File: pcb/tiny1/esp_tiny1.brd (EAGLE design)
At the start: 45 x 95 mm, 35 parts, among them IC1 4000D, Q1 BUZ11BH

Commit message: added tiny board
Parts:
- removed D3: ES2D, diode:SMB
- removed DHT22: TEMP-HUM-SENSOR-DHT22, diy-modules:TEMP-HUM-SENSOR-DHT22
- removed ESP: ESP12E_DEVKIT, ESP12E_DEVKIT:ESP12E_DEVKIT
- removed IC1: 4000D, 40xx:SO14
- removed LDO: REG1117, burr-brown:SOT223
- removed PIR: MOTION-PIR-DYP-ME003, diy-modules:MOTION-PIR-DYP-ME003
- removed Q1: BUZ11BH, transistor-power:TO220BH
- removed SV2, SV3: (no value), con-lstb:MA03-1
- removed TP1: TPTP20SQ, testpad:TP20SQ
- removed U$5, U$6: SMD_SJ_3WAY_CLOSED, JKW_CHIP:SMD_SJ_3WAY_CLOSED
- added D1: (no value), SparkFun-LED:WS2812B
- added DS_GND, DS_SIG, DS_VCC: (no value), wirepad:SMD1,27-2,54
- added PIR1: MOTION-PIR-DYP-ME003, diy-modules:MOTION-PIR-DYP-ME003_FRAMELESS
- added R4, R5, R6: 10k, rcl:M0805
- added S1: TAC_SWITCHSMD, SparkFun-Retired:TACTILE-SWITCH-SMD
- added U1: (no value), esp8266modules:ESP12-SMD
- U$12: value MP1584EN_FRAMELESS -> MP1584EN; device JKW_CHIP:MP1584EN_FRAMELESS -> JKW_CHIP:MP1584EN
- moved U$4 104.6 mm to (96.2, 22.7)
- moved SV4 98.5 mm to (87.2, 37.2), turned to 270 degrees
- moved R1 97.9 mm to (94.8, 37.5)
- moved T_DIM1 94.0 mm to (100.0, 12.5), turned to 0 degrees
- moved U$11 88.6 mm to (62.8, 13.6)
- moved U$9 85.8 mm to (79.6, 23.7), flipped to the top
- moved DP2 80.5 mm to (93.5, 13.5), turned to 180 degrees
- moved SV1 76.6 mm to (67.5, 41.8), flipped to the bottom, turned to 0 degrees
- moved RELAY1 76.6 mm to (68.0, 18.9), turned to 270 degrees
- moved T_DIM2 74.7 mm to (92.5, 12.5), turned to 0 degrees
- moved D8 70.8 mm to (77.6, 20.1)
- moved U$3 70.0 mm to (100.0, 4.50), turned to 0 degrees
- moved U$1 61.5 mm to (80.7, 28.9)
- moved U$8 59.5 mm to (60.0, 4.50), turned to 0 degrees
- moved DP3 59.0 mm to (85.1, 13.5), turned to 180 degrees
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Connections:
- removed net DIMM2: DP2.1, ESP.D1, ESP.D11
- removed net N$12: ESP.EN, ESP.EN1
- removed net N$13: ESP.RST, ESP.RST1
- removed net N$14: D3.A, ESP.RSV@1, ESP.RSV@11
- removed net N$24: PIR.4, U$5.1
- removed net N$31: PIR.1, U$6.3
- removed net PIR: ESP.D3, ESP.D31, PIR.2
- removed net RERLAY: ESP.D6, ESP.D61, RELAY.1
- new net A_IN: U$3.P$2, U1.ADC
- new net N$5: PIR1.2, U1.GPIO14
- new net N$6: SV1.2, U1.RXD0
- new net N$7: S1.1, U1.GPIO0
- new net RELAY: RELAY.1, U1.GPIO12
- net DHT_SIG/SDA: now also U1.GPIO2; no longer DHT22.2, ESP.D4, ESP.D41
- net DIMM1: now also U1.GPIO4; no longer ESP.D2, ESP.D21, IC1.5, Q1.G
- net DIMM3: now also D1.4, U1.GPIO16; no longer ESP.D0, ESP.D01, IC1.3
- net DIMMING1: no longer Q1.D
- net EARTH_HUM_POW: now also R5.1, U1.GPIO15; no longer ESP.D8, ESP.D81
- net GND: now also D1.3, DS_GND.1, PIR1.3, R5.2, S1.3, SV1.1, U1.GND; no longer DHT22.4, ESP.GND@0, ESP.GND@1, ESP.GND@2, ESP.GND@3, ESP.GND@4, ESP.GND@5, ESP.GND@6, ESP.GND@7, IC1.7, LDO.1, PIR.3, Q1.S, SV1.3, SV2.3, SV3.3
- net N$1: now also R6.1, U1.CH_PD; no longer ESP.AD0, ESP.AD1, U$3.P$2
- net N$17: no longer LDO.3
- net N$2: now also R4.1, U1.RESET; no longer ESP.RSV@0, ESP.RSV@01
- net N$4: now also SV1.3, U1.TXD0; no longer IC1.6, TP1.TP
- net ONEWIRE_DS12B20: now also DS_SIG.1, U1.GPIO13; no longer ESP.D7, ESP.D71, SV1.2, SV2.2, SV3.2
- net SCL: now also DP2.1, U1.GPIO5; no longer ESP.D5, ESP.D51
- net VCC: now also PIR1.1; no longer D3.C, D8.C, ESP.VIN, ESP.VIN1, LDO.2, RELAY1.COIL0, U$12.VOUT, U$6.2
- net VDD: now also D1.1, D8.C, DS_VCC.1, PIR1.4, R4.2, R6.2, RELAY1.COIL0, U$12.VOUT, U1.VCC; no longer DHT22.1, ESP.3V3@0, ESP.3V3@1, ESP.3V3@2, ESP.3V3@3, ESP.3V3@4, ESP.3V3@5, IC1.14, SV1.1, SV2.1, SV3.1, U$5.2
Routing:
- net VCC: track 123.5 -> 0.00 mm, vias 4 -> 0
- net DHT_SIG/SDA: track 138.4 -> 20.4 mm, vias 2 -> 1
- net VDD: track 194.7 -> 94.9 mm, vias 3 -> 1
- net A_IN: track 0.00 -> 81.1 mm
- net ONEWIRE_DS12B20: track 94.0 -> 28.7 mm, vias 5 -> 0
- net GND: track 64.1 -> 5.33 mm, vias 15 -> 3
- net PIR: track 58.3 -> 0.00 mm, vias 3 -> 0
- net DIMM2: track 58.3 -> 0.00 mm, vias 2 -> 0
- net DIMMING1: track 69.3 -> 11.6 mm
- net N$1: track 42.2 -> 4.45 mm
- net EARTH_HUM_POW: track 12.2 -> 47.8 mm, vias 0 -> 1
- net NORMALLY_OPEN: track 40.1 -> 7.55 mm
- net RERLAY: track 31.4 -> 0.00 mm, vias 1 -> 0
- net DIMMING2: track 40.4 -> 10.6 mm
- net SCL: track 82.5 -> 57.9 mm
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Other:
- board size 45 x 95 mm -> 50 x 50 mm
- board text added: "SMARTHOME ESPtiny v01 | 2017"
- board text removed: "DIM1"
- board text removed: "DIM2"
- board text removed: "DIM3"
- board text removed: "POWER VIA 3V"
- board text removed: "POWER VIA VIN"
- board text removed: "SIG"
- board text removed: "SMARTHOME ESP MQTT v03 | 2017"

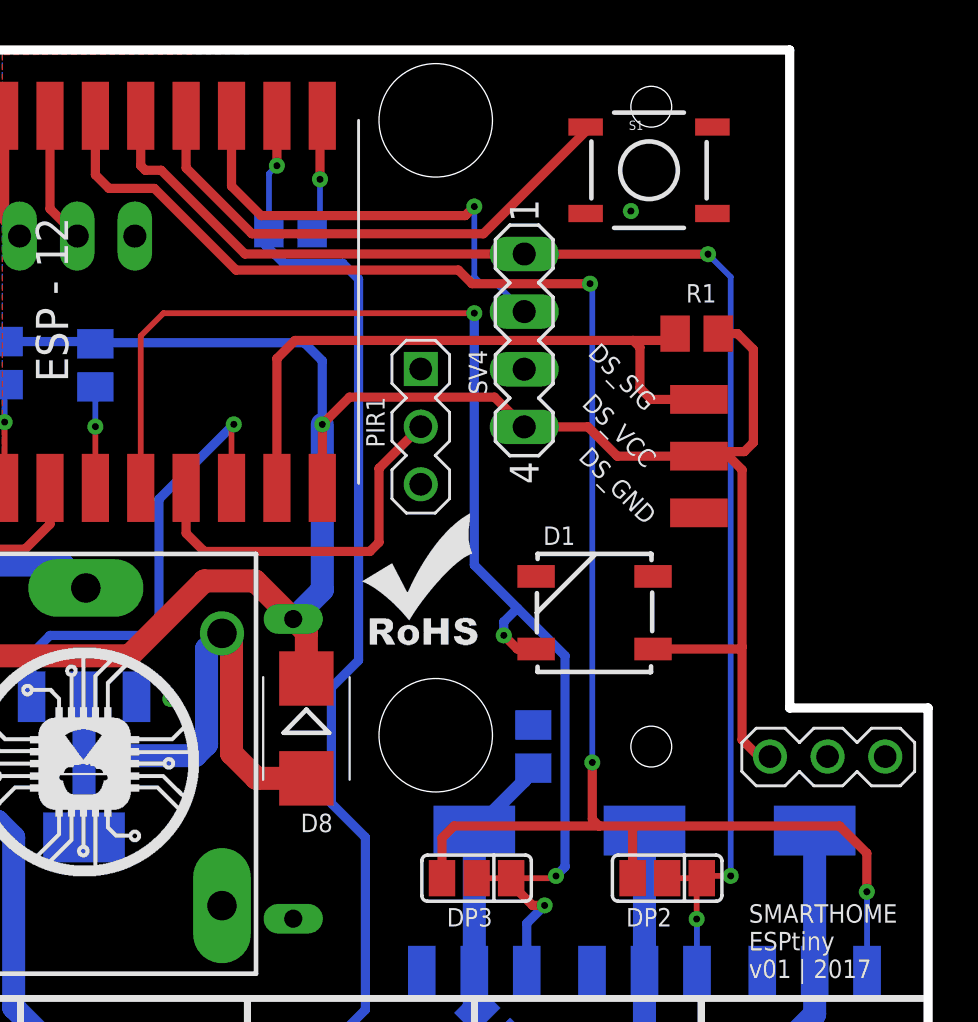
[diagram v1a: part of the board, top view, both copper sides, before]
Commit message: fixed i2c error, thanks to michell
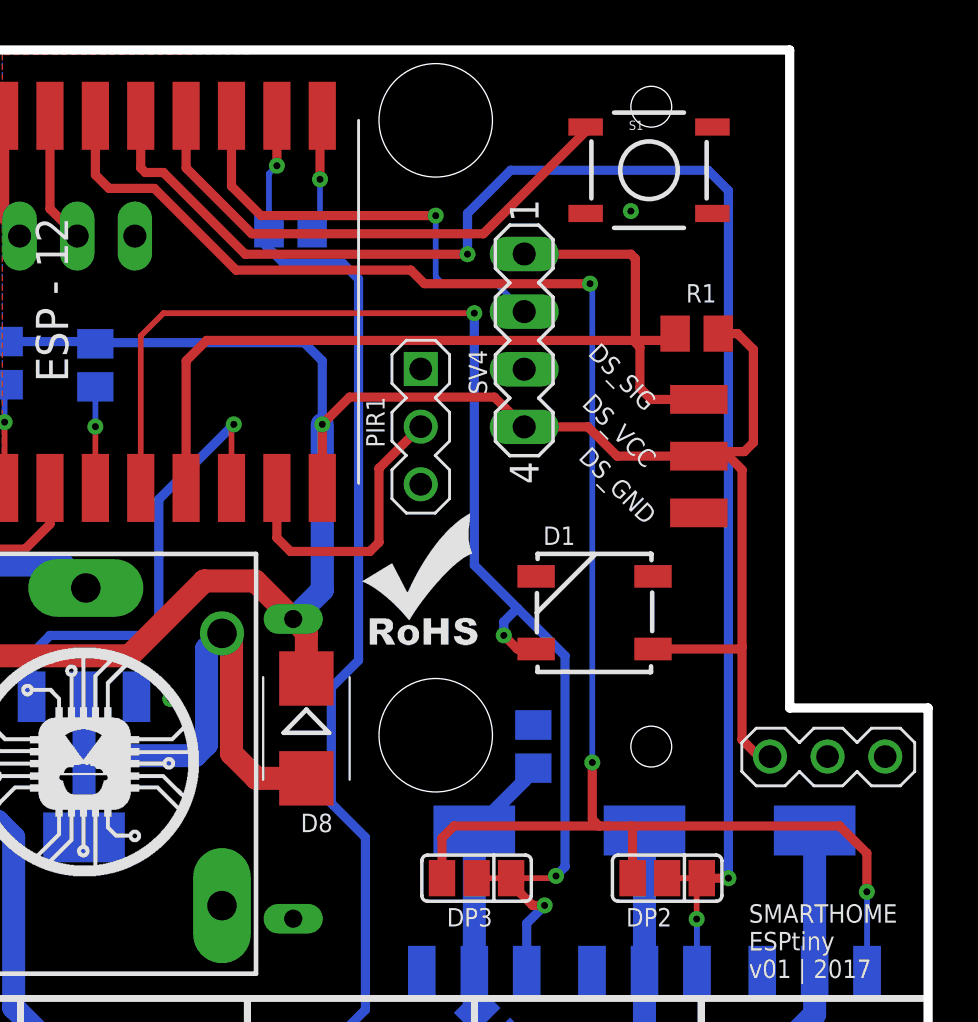
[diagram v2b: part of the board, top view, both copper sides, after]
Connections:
- removed net N$5: PIR1.2, U1.GPIO14
- removed net ONEWIRE_DS12B20: DS_SIG.1, R1.1, U1.GPIO13
- new net N$8: DP2.1, U1.GPIO5
- new net PIR: PIR1.2, U1.GPIO13
- net SCL: now also DS_SIG.1, R1.1, U1.GPIO14; no longer DP2.1, U1.GPIO5
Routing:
- net N$8: track 0.00 -> 64.2 mm, vias 0 -> 2
- net ONEWIRE_DS12B20: track 28.7 -> 0.00 mm
- net N$5: track 16.9 -> 0.00 mm
- net SCL: track 57.9 -> 41.3 mm, vias 2 -> 0
- net PIR: track 0.00 -> 13.0 mm
- net DHT_SIG/SDA: track 20.4 -> 19.9 mm
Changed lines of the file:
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@@
 <contactref element="SV4" pad="2"/>
 <contactref element="U1" pad="GPIO2"/>
-<via x="85" y="43.1" extent="1-16" drill="0.3048"/>
-<wire x1="85" y1="43.1" x2="85" y2="40" width="0.254" layer="16"/>
-<wire x1="85" y1="40" x2="85.3" y2="39.7" width="0.254" layer="16"/>
-<wire x1="85.3" y1="39.7" x2="85.97" y2="39.7" width="0.254" layer="16"/>
+<via x="83.3" y="42.7" extent="1-16" drill="0.3048"/>
 <wire x1="85.97" y1="39.7" x2="87.2" y2="38.47" width="0.254" layer="16"/>
 <wire x1="74.3" y1="47.1" x2="74.3" y2="44" width="0.4064" layer="1"/>
 <wire x1="74.3" y1="44" x2="75.6" y2="42.7" width="0.4064" layer="1"/>
-<wire x1="75.6" y1="42.7" x2="84.6" y2="42.7" width="0.4064" layer="1"/>
-<wire x1="84.6" y1="42.7" x2="85" y2="43.1" width="0.4064" layer="1"/>
+<wire x1="75.6" y1="42.7" x2="83.3" y2="42.7" width="0.4064" layer="1"/>
+<wire x1="85.97" y1="39.7" x2="83.6" y2="39.7" width="0.254" layer="16"/>
+<wire x1="83.6" y1="39.7" x2="83.3" y2="40" width="0.254" layer="16"/>
+<wire x1="83.3" y1="40" x2="83.3" y2="42.7" width="0.254" layer="16"/>
 </signal>
 <signal name="DIMM1">
@@
 <wire x1="83.576" y1="15.276" x2="84.1" y2="15.8" width="0.4064" layer="1"/>
 <wire x1="84.1" y1="15.8" x2="90.5" y2="15.8" width="0.4064" layer="1"/>
-<wire x1="90.5" y1="15.8" x2="101.1" y2="15.8" width="0.4064" layer="1"/>
+<wire x1="90.5" y1="15.8" x2="90.9" y2="15.8" width="0.4064" layer="1"/>
+<wire x1="91.9" y1="15.8" x2="101.1" y2="15.8" width="0.4064" layer="1"/>
 <wire x1="101.1" y1="15.8" x2="102.3" y2="14.6" width="0.4064" layer="1"/>
 <wire x1="90.2" y1="18.6" x2="90.2" y2="16.1" width="0.4064" layer="1"/>
@@
 <wire x1="68.9" y1="43.9" x2="70.9" y2="43.9" width="0.4064" layer="1"/>
 <wire x1="70.9" y1="43.9" x2="74.5" y2="40.3" width="0.4064" layer="1"/>
-<wire x1="74.5" y1="40.3" x2="84.3" y2="40.3" width="0.4064" layer="1"/>
-<wire x1="84.3" y1="40.3" x2="84.9" y2="39.7" width="0.4064" layer="1"/>
-<wire x1="84.9" y1="39.7" x2="90.1" y2="39.7" width="0.4064" layer="1"/>
-<wire x1="90.5" y1="15.8" x2="91.9" y2="15.8" width="0" layer="19" extent="1-1"/>
+<wire x1="74.5" y1="40.3" x2="82.2" y2="40.3" width="0.4064" layer="1"/>
+<wire x1="82.2" y1="40.3" x2="82.8" y2="39.7" width="0.4064" layer="1"/>
+<wire x1="82.8" y1="39.7" x2="90.1" y2="39.7" width="0.4064" layer="1"/>
+<wire x1="91.9" y1="15.8" x2="90.9" y2="15.8" width="0.4064" layer="1"/>
 </signal>
 <signal name="DIMM3">
@@
 <wire x1="97.5" y1="5" x2="100" y2="7.5" width="1.016" layer="16"/>
 <wire x1="100" y1="7.5" x2="100" y2="9.401" width="1.016" layer="16"/>
-</signal>
-<signal name="ONEWIRE_DS12B20">
-<contactref element="R1" pad="1"/>
-<contactref element="U1" pad="GPIO13"/>
-<contactref element="DS_SIG" pad="1"/>
-<wire x1="76.3" y1="30.7" x2="76.3" y2="36.4" width="0.4064" layer="1"/>
-<wire x1="76.3" y1="36.4" x2="77.1" y2="37.2" width="0.4064" layer="1"/>
-<wire x1="77.1" y1="37.2" x2="92" y2="37.2" width="0.4064" layer="1"/>
-<wire x1="92" y1="37.2" x2="93.55" y2="37.2" width="0.4064" layer="1"/>
-<wire x1="93.55" y1="37.2" x2="93.85" y2="37.5" width="0.4064" layer="1"/>
-<wire x1="94.9" y1="34.6" x2="92.8" y2="34.6" width="0.4064" layer="1"/>
-<wire x1="92.8" y1="34.6" x2="92.3" y2="35.1" width="0.4064" layer="1"/>
-<wire x1="92.3" y1="35.1" x2="92.3" y2="36.9" width="0.4064" layer="1"/>
-<wire x1="92.3" y1="36.9" x2="92" y2="37.2" width="0.4064" layer="1"/>
 </signal>
 <signal name="N$17">
@@
 <wire x1="64.3" y1="33.6" x2="64.3" y2="35.25" width="0.254" layer="16"/>
 </signal>
-<signal name="N$5">
+<signal name="PIR">
 <contactref element="PIR1" pad="2"/>
-<contactref element="U1" pad="GPIO14"/>
-<wire x1="72.3" y1="30.7" x2="72.3" y2="28.7" width="0.4064" layer="1"/>
-<wire x1="72.3" y1="28.7" x2="73.1" y2="27.9" width="0.4064" layer="1"/>
-<wire x1="73.1" y1="27.9" x2="80.4" y2="27.9" width="0.4064" layer="1"/>
 <wire x1="80.4" y1="27.9" x2="80.8" y2="28.3" width="0.4064" layer="1"/>
 <wire x1="80.8" y1="28.3" x2="80.8" y2="31.56" width="0.4064" layer="1"/>
 <wire x1="80.8" y1="31.56" x2="82.64" y2="33.4" width="0.4064" layer="1"/>
+<contactref element="U1" pad="GPIO13"/>
+<wire x1="80.4" y1="27.9" x2="76.9" y2="27.9" width="0.4064" layer="1"/>
+<wire x1="76.9" y1="27.9" x2="76.3" y2="28.5" width="0.4064" layer="1"/>
+<wire x1="76.3" y1="28.5" x2="76.3" y2="30.7" width="0.4064" layer="1"/>
 </signal>
 <signal name="RELAY">
@@
 <wire x1="71.1" y1="25" x2="71.1" y2="30.2" width="0.4064" layer="16"/>
 </signal>
-<signal name="SCL">
-<contactref element="DP2" pad="1"/>
-<contactref element="SV4" pad="1"/>
-<contactref element="U1" pad="GPIO5"/>
-<wire x1="95.024" y1="13.5" x2="95.124" y2="13.6" width="0.254" layer="1"/>
-<wire x1="95.124" y1="13.6" x2="96.3" y2="13.6" width="0.254" layer="1"/>
-<via x="96.3" y="13.6" extent="1-16" drill="0.3048"/>
-<wire x1="96.3" y1="13.6" x2="96.3" y2="40" width="0.254" layer="16"/>
-<wire x1="96.3" y1="40" x2="95.3" y2="41" width="0.254" layer="16"/>
-<via x="95.3" y="41" extent="1-16" drill="0.3048"/>
-<wire x1="74.89" y1="41.01" x2="87.2" y2="41.01" width="0.4064" layer="1"/>
-<wire x1="87.2" y1="41.01" x2="87.21" y2="41" width="0.4064" layer="1"/>
-<wire x1="87.21" y1="41" x2="95.3" y2="41" width="0.4064" layer="1"/>
-<wire x1="74.89" y1="41.01" x2="71.2" y2="44.7" width="0.4064" layer="1"/>
-<wire x1="71.2" y1="44.7" x2="70.5" y2="44.7" width="0.4064" layer="1"/>
-<wire x1="70.5" y1="44.7" x2="70.3" y2="44.9" width="0.4064" layer="1"/>
-<wire x1="70.3" y1="44.9" x2="70.3" y2="47.1" width="0.4064" layer="1"/>
-</signal>
 <signal name="N$1">
 <contactref element="U1" pad="CH_PD"/>
@@
 <wire x1="89.906" y1="46.406" x2="89.906" y2="46.605" width="0.4064" layer="1"/>
 </signal>
+<signal name="N$8">
+<contactref element="DP2" pad="1"/>
+<contactref element="U1" pad="GPIO5"/>
+<wire x1="95.024" y1="13.5" x2="96.2" y2="13.5" width="0.4064" layer="1"/>
+<via x="96.2" y="13.5" extent="1-16" drill="0.3048"/>
+<wire x1="96.2" y1="13.5" x2="96.2" y2="43.8" width="0.4064" layer="16"/>
+<wire x1="96.2" y1="43.8" x2="95.3" y2="44.7" width="0.4064" layer="16"/>
+<wire x1="95.3" y1="44.7" x2="86.6" y2="44.7" width="0.4064" layer="16"/>
+<via x="84.7" y="41" extent="1-16" drill="0.3048"/>
+<wire x1="84.7" y1="41" x2="74.9" y2="41" width="0.4064" layer="1"/>
+<wire x1="74.9" y1="41" x2="71.3" y2="44.6" width="0.4064" layer="1"/>
+<wire x1="71.3" y1="44.6" x2="70.5" y2="44.6" width="0.4064" layer="1"/>
+<wire x1="70.5" y1="44.6" x2="70.3" y2="44.8" width="0.4064" layer="1"/>
+<wire x1="70.3" y1="44.8" x2="70.3" y2="47.1" width="0.4064" layer="1"/>
+<wire x1="86.6" y1="44.7" x2="84.7" y2="42.8" width="0.4064" layer="16"/>
+<wire x1="84.7" y1="42.8" x2="84.7" y2="41" width="0.4064" layer="16"/>
+</signal>
+<signal name="SCL">
+<contactref element="R1" pad="1"/>
+<contactref element="DS_SIG" pad="1"/>
+<contactref element="SV4" pad="1"/>
+<contactref element="U1" pad="GPIO14"/>
+<wire x1="73.2" y1="37.2" x2="92" y2="37.2" width="0.4064" layer="1"/>
+<wire x1="92" y1="37.2" x2="93.55" y2="37.2" width="0.4064" layer="1"/>
+<wire x1="93.55" y1="37.2" x2="93.85" y2="37.5" width="0.4064" layer="1"/>
+<wire x1="94.9" y1="34.6" x2="92.8" y2="34.6" width="0.4064" layer="1"/>
+<wire x1="92.8" y1="34.6" x2="92.3" y2="35.1" width="0.4064" layer="1"/>
+<wire x1="92.3" y1="35.1" x2="92.3" y2="36.9" width="0.4064" layer="1"/>
+<wire x1="92.3" y1="36.9" x2="92" y2="37.2" width="0.4064" layer="1"/>
+<wire x1="87.2" y1="41.01" x2="87.21" y2="41" width="0.4064" layer="1"/>
+<wire x1="72.3" y1="30.7" x2="72.3" y2="36.3" width="0.4064" layer="1"/>
+<wire x1="72.3" y1="36.3" x2="73.2" y2="37.2" width="0.4064" layer="1"/>
+<wire x1="87.21" y1="41" x2="91.9" y2="41" width="0.4064" layer="1"/>
+<wire x1="91.9" y1="41" x2="92.1" y2="40.8" width="0.4064" layer="1"/>
+<wire x1="92.1" y1="40.8" x2="92.1" y2="37.3" width="0.4064" layer="1"/>
+<wire x1="92.1" y1="37.3" x2="92" y2="37.2" width="0.4064" layer="1"/>
+</signal>
 </signals>
